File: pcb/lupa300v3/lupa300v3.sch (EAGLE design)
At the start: 38 parts

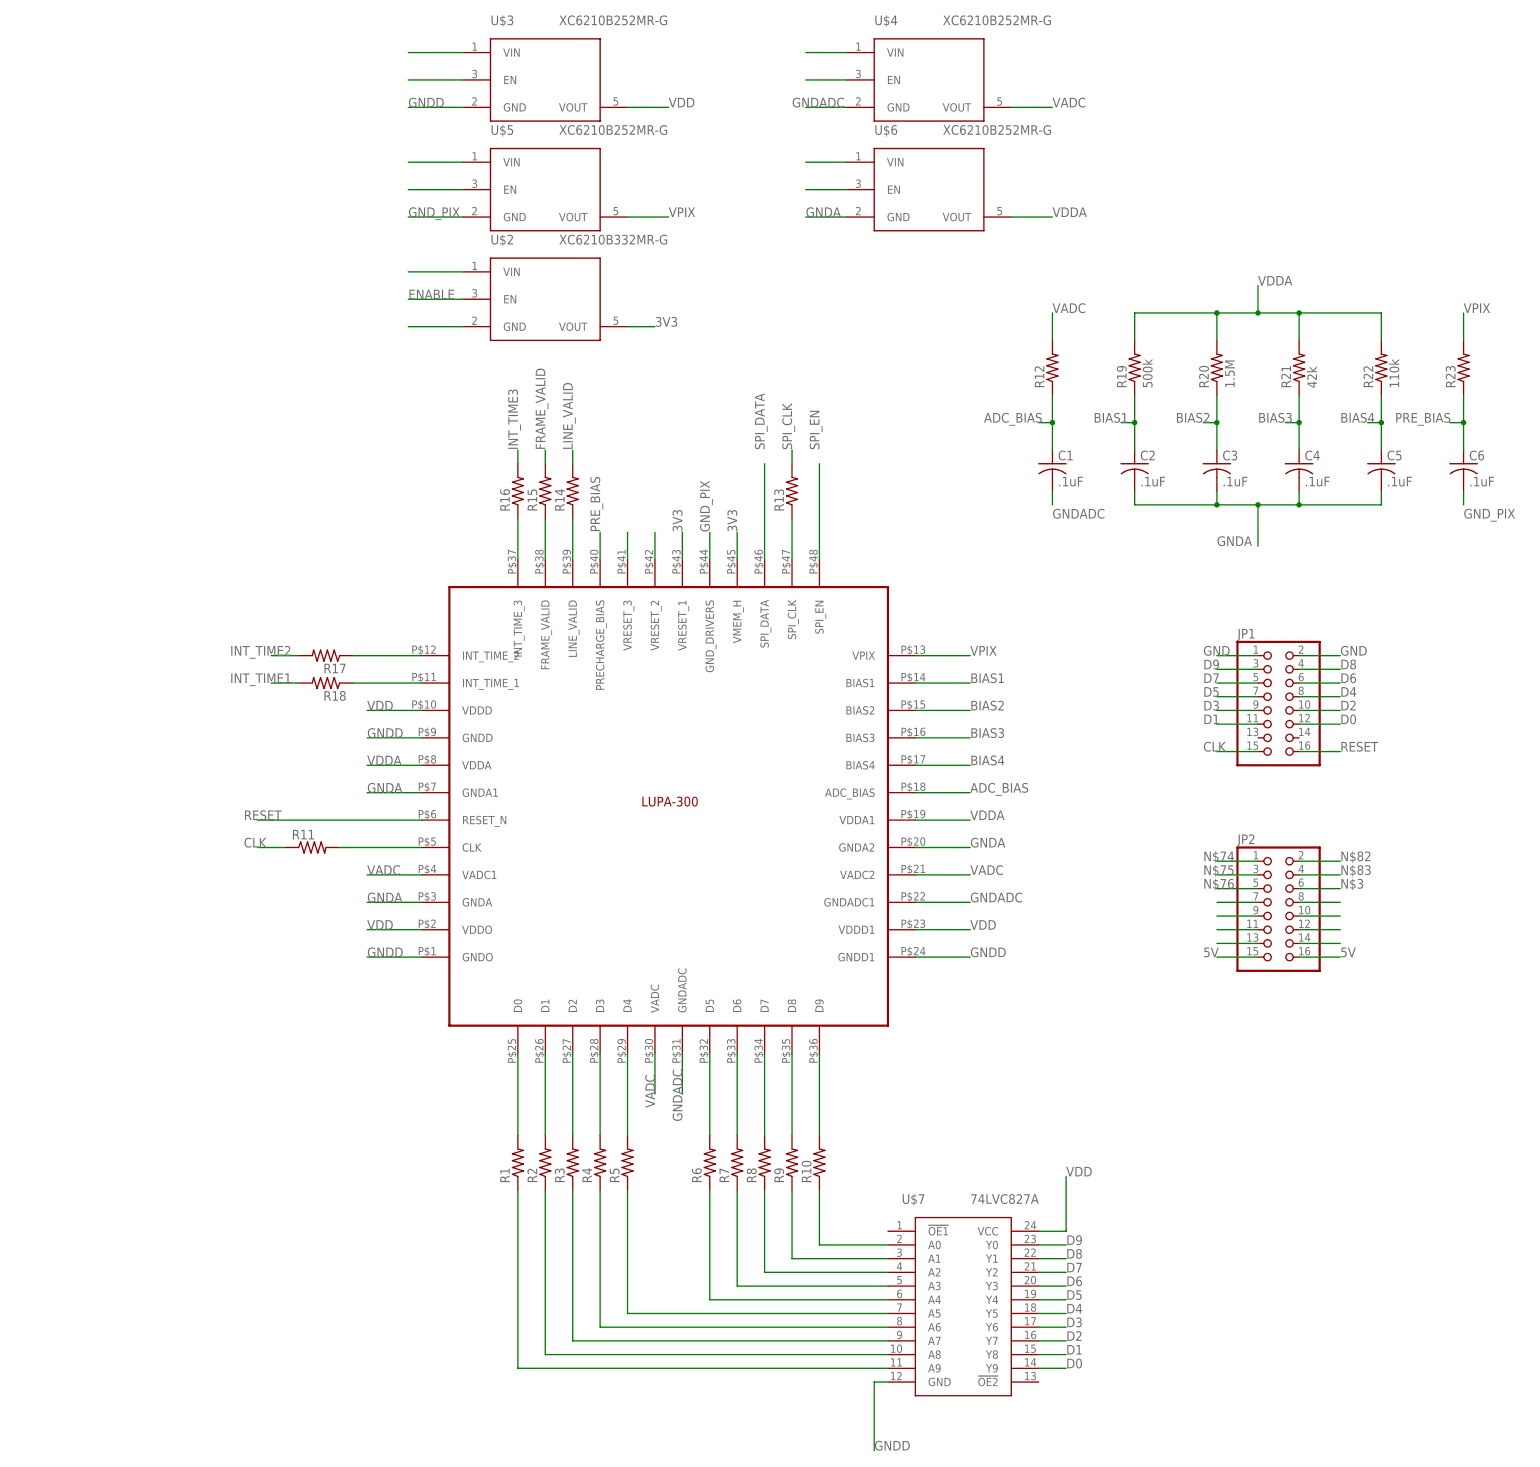
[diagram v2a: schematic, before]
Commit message: added separate ground planes
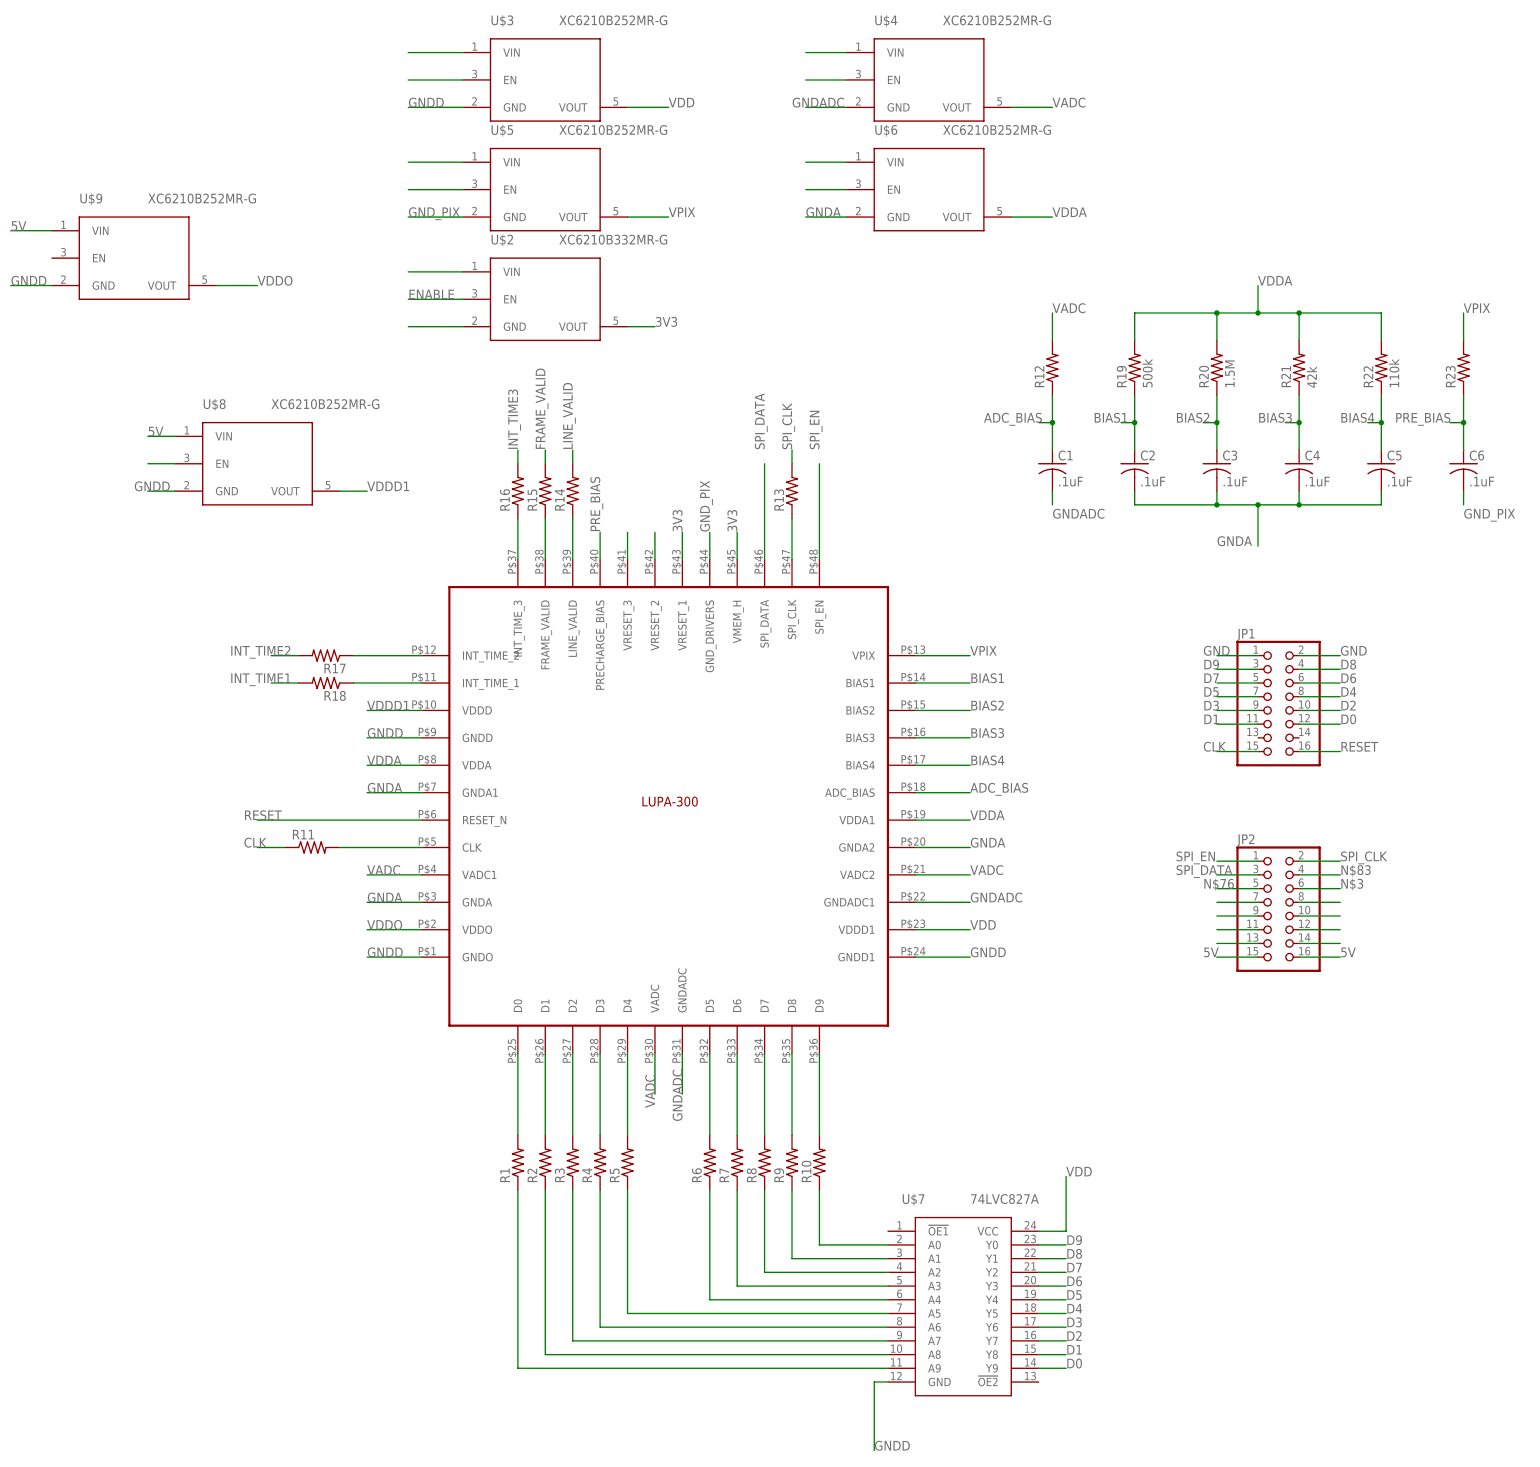
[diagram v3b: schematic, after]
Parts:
- added U$8, U$9: XC6210B252MR-G, lupa300-components:XC6210B252MR-G
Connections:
- removed net N$74: JP2.1
- removed net N$75: JP2.3
- removed net N$82: JP2.2
- new net N$40: U$8.EN
- new net VDDD1: U$1.VDDD, U$8.VOUT
- new net VDDO: U$1.VDDO, U$9.VOUT
- net 5V: now also U$8.VIN, U$9.VIN
- net GNDD: now also U$8.GND, U$9.GND
- net SPI_CLK: now also JP2.2
- net SPI_DATA: now also JP2.3
- net SPI_EN: now also JP2.1
- net VDD: no longer U$1.VDDD, U$1.VDDO
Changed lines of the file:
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@@
 <?xml version="1.0" encoding="utf-8"?>
 <!DOCTYPE eagle SYSTEM "eagle.dtd">
-<eagle version="8.6.1">
+<eagle version="8.7.0">
 <drawing>
 <settings>
@@
 <part name="C6" library="rcl" library_urn="urn:adsk.eagle:library:334" deviceset="C-US" device="C0603K" package3d_urn="urn:adsk.eagle:package:23680/2" value=".1uF"/>
 <part name="U$7" library="lupa300-components" deviceset="74LVC827A" device=""/>
+<part name="U$8" library="lupa300-components" deviceset="XC6210B252MR-G" device=""/>
+<part name="U$9" library="lupa300-components" deviceset="XC6210B252MR-G" device=""/>
 </parts>
 <sheets>
@@
 <instance part="C6" gate="G$1" x="228.6" y="142.24"/>
 <instance part="U$7" gate="G$1" x="127" y="-30.48"/>
+<instance part="U$8" gate="G$1" x="-5.08" y="134.62"/>
+<instance part="U$9" gate="G$1" x="-27.94" y="172.72"/>
 </instances>
 <busses>
@@
 </segment>
 <segment>
-<pinref part="U$1" gate="G$1" pin="VDDD"/>
-<wire x1="35.56" y1="96.52" x2="25.4" y2="96.52" width="0.1524" layer="91"/>
-<label x="25.4" y="96.52" size="1.778" layer="95"/>
-</segment>
-<segment>
 <pinref part="U$1" gate="G$1" pin="VDDD1"/>
 <wire x1="127" y1="55.88" x2="137.16" y2="55.88" width="0.1524" layer="91"/>
 <label x="137.16" y="55.88" size="1.778" layer="95"/>
-</segment>
-<segment>
-<pinref part="U$1" gate="G$1" pin="VDDO"/>
-<wire x1="35.56" y1="55.88" x2="25.4" y2="55.88" width="0.1524" layer="91"/>
-<label x="25.4" y="55.88" size="1.778" layer="95"/>
 </segment>
 <segment>
@@
 <net name="GNDD" class="0">
 <segment>
-<pinref part="U$1" gate="G$1" pin="GNDD"/>
-<wire x1="35.56" y1="91.44" x2="25.4" y2="91.44" width="0.1524" layer="91"/>
-<label x="25.4" y="91.44" size="1.778" layer="95"/>
-</segment>
-<segment>
 <pinref part="U$1" gate="G$1" pin="GNDD1"/>
 <wire x1="127" y1="50.8" x2="137.16" y2="50.8" width="0.1524" layer="91"/>
@@
 <label x="119.38" y="-40.64" size="1.778" layer="95"/>
 </segment>
+<segment>
+<pinref part="U$1" gate="G$1" pin="GNDD"/>
+<wire x1="35.56" y1="91.44" x2="25.4" y2="91.44" width="0.1524" layer="91"/>
+<label x="25.4" y="91.44" size="1.778" layer="95"/>
+</segment>
+<segment>
+<pinref part="U$8" gate="G$1" pin="GND"/>
+<wire x1="-10.16" y1="137.16" x2="-15.24" y2="137.16" width="0.1524" layer="91"/>
+<label x="-17.78" y="137.16" size="1.778" layer="95"/>
+</segment>
+<segment>
+<pinref part="U$9" gate="G$1" pin="GND"/>
+<wire x1="-33.02" y1="175.26" x2="-40.64" y2="175.26" width="0.1524" layer="91"/>
+<label x="-40.64" y="175.26" size="1.778" layer="95"/>
+</segment>
 </net>
 <net name="N$1" class="0">
@@
 </segment>
 </net>
-<net name="N$74" class="0">
-<segment>
-<pinref part="JP2" gate="A" pin="1"/>
-<wire x1="190.5" y1="68.58" x2="182.88" y2="68.58" width="0.1524" layer="91"/>
-<label x="180.34" y="68.58" size="1.778" layer="95"/>
-</segment>
-</net>
-<net name="N$75" class="0">
-<segment>
-<pinref part="JP2" gate="A" pin="3"/>
-<wire x1="190.5" y1="66.04" x2="182.88" y2="66.04" width="0.1524" layer="91"/>
-<label x="180.34" y="66.04" size="1.778" layer="95"/>
-</segment>
-</net>
 <net name="N$76" class="0">
 <segment>
@@
 <label x="104.14" y="144.78" size="1.778" layer="95" rot="R90"/>
 </segment>
-</net>
-<net name="N$82" class="0">
 <segment>
 <pinref part="JP2" gate="A" pin="2"/>
@@
 <label x="205.74" y="50.8" size="1.778" layer="95"/>
 </segment>
+<segment>
+<pinref part="U$8" gate="G$1" pin="VIN"/>
+<wire x1="-10.16" y1="147.32" x2="-15.24" y2="147.32" width="0.1524" layer="91"/>
+<label x="-15.24" y="147.32" size="1.778" layer="95"/>
+</segment>
+<segment>
+<pinref part="U$9" gate="G$1" pin="VIN"/>
+<wire x1="-33.02" y1="185.42" x2="-40.64" y2="185.42" width="0.1524" layer="91"/>
+<label x="-40.64" y="185.42" size="1.778" layer="95"/>
+</segment>
 </net>
 <net name="INT_TIME2" class="0">
@@
 <label x="99.06" y="144.78" size="1.778" layer="95" rot="R90"/>
 </segment>
+<segment>
+<pinref part="JP2" gate="A" pin="3"/>
+<wire x1="190.5" y1="66.04" x2="182.88" y2="66.04" width="0.1524" layer="91"/>
+<label x="175.26" y="66.04" size="1.778" layer="95"/>
+</segment>
 </net>
 <net name="SPI_EN" class="0">
@@
 <wire x1="109.22" y1="124.46" x2="109.22" y2="142.24" width="0.1524" layer="91"/>
 <label x="109.22" y="144.78" size="1.778" layer="95" rot="R90"/>
+</segment>
+<segment>
+<pinref part="JP2" gate="A" pin="1"/>
+<wire x1="190.5" y1="68.58" x2="182.88" y2="68.58" width="0.1524" layer="91"/>
+<label x="175.26" y="68.58" size="1.778" layer="95"/>
 </segment>
 </net>
@@
 </segment>
 </net>
+<net name="VDDD1" class="0">
+<segment>
+<pinref part="U$8" gate="G$1" pin="VOUT"/>
+<wire x1="20.32" y1="137.16" x2="25.4" y2="137.16" width="0.1524" layer="91"/>
+<label x="25.4" y="137.16" size="1.778" layer="95"/>
+</segment>
+<segment>
+<pinref part="U$1" gate="G$1" pin="VDDD"/>
+<wire x1="35.56" y1="96.52" x2="25.4" y2="96.52" width="0.1524" layer="91"/>
+<label x="25.4" y="96.52" size="1.778" layer="95"/>
+</segment>
+</net>
+<net name="N$40" class="0">
+<segment>
+<pinref part="U$8" gate="G$1" pin="EN"/>
+<wire x1="-10.16" y1="142.24" x2="-15.24" y2="142.24" width="0.1524" layer="91"/>
+</segment>
+</net>
+<net name="VDDO" class="0">
+<segment>
+<pinref part="U$1" gate="G$1" pin="VDDO"/>
+<wire x1="35.56" y1="55.88" x2="25.4" y2="55.88" width="0.1524" layer="91"/>
+<label x="25.4" y="55.88" size="1.778" layer="95"/>
+</segment>
+<segment>
+<pinref part="U$9" gate="G$1" pin="VOUT"/>
+<wire x1="-2.54" y1="175.26" x2="5.08" y2="175.26" width="0.1524" layer="91"/>
+<label x="5.08" y="175.26" size="1.778" layer="95"/>
+</segment>
+</net>
